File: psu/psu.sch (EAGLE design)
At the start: 7 parts

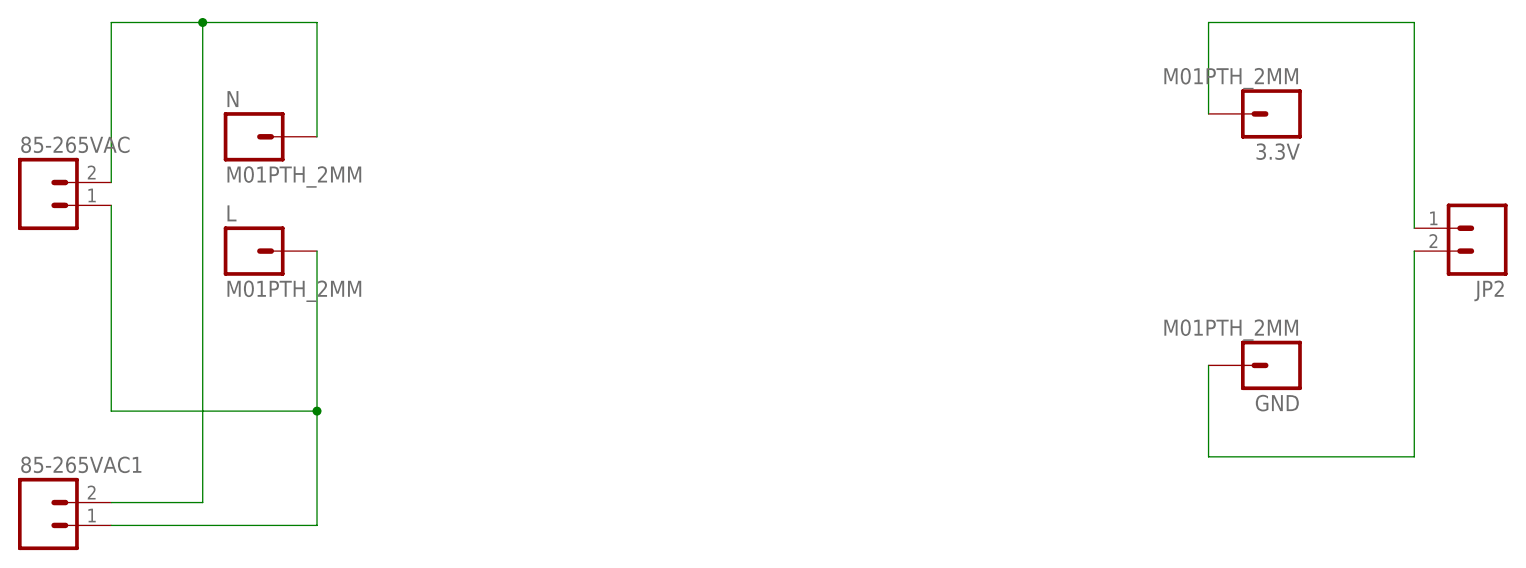
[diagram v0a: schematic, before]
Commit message: psu pcb: smaller holes for psu module
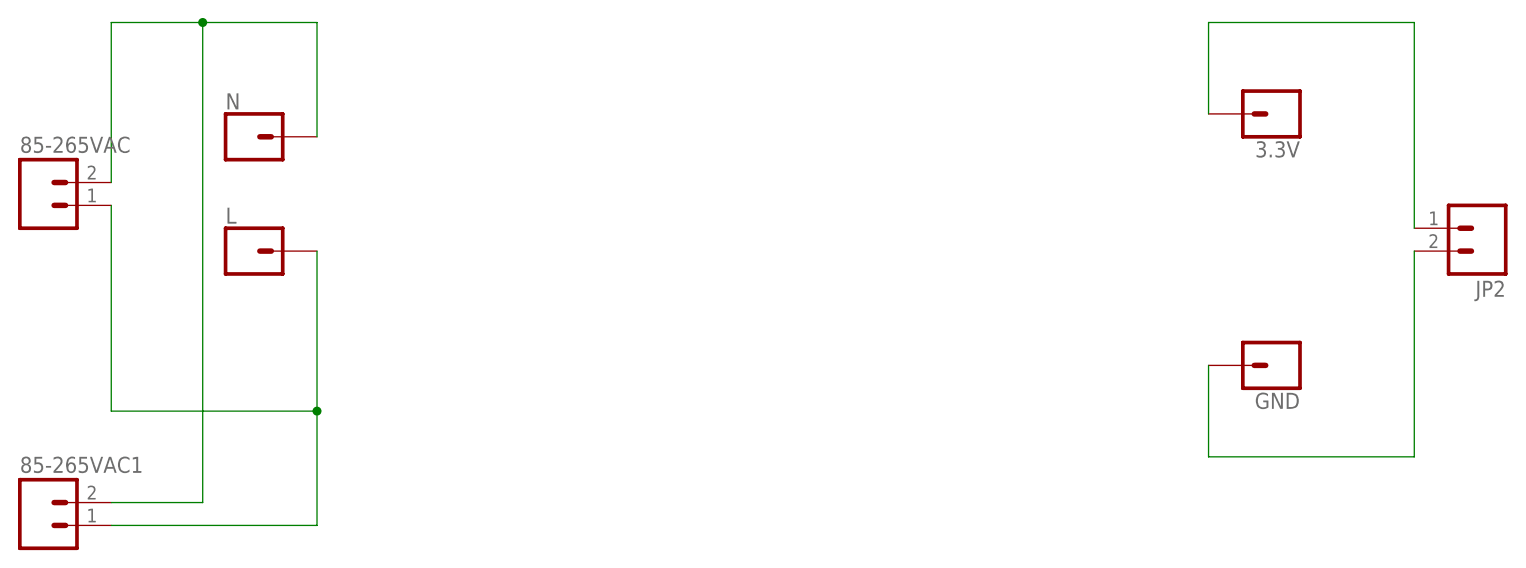
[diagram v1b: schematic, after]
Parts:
- 3.3V, GND, L, N: value M01PTH_2MM -> (none); device SparkFun (old):M01PTH_2MM -> 1X01:CONN_01PTH_1.4MM
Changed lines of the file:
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@@
 <?xml version="1.0" encoding="utf-8"?>
 <!DOCTYPE eagle SYSTEM "eagle.dtd">
-<eagle version="7.2.0">
+<eagle version="8.7.1">
 <drawing>
 <settings>
-<setting alwaysvectorfont="yes"/>
+<setting alwaysvectorfont="no"/>
+<setting keepoldvectorfont="yes"/>
 <setting verticaltext="up"/>
 </settings>
@@
 <layer number="54" name="bGND_GNDA" color="1" fill="9" visible="no" active="no"/>
 <layer number="56" name="wert" color="7" fill="1" visible="no" active="no"/>
+<layer number="57" name="tCAD" color="7" fill="1" visible="no" active="no"/>
+<layer number="59" name="tCarbon" color="7" fill="1" visible="no" active="no"/>
+<layer number="60" name="bCarbon" color="7" fill="1" visible="no" active="no"/>
 <layer number="90" name="Modules" color="5" fill="1" visible="yes" active="yes"/>
 <layer number="91" name="Nets" color="2" fill="1" visible="yes" active="yes"/>
@@
 <layer number="97" name="Info" color="7" fill="1" visible="yes" active="yes"/>
 <layer number="98" name="Guide" color="6" fill="1" visible="yes" active="yes"/>
+<layer number="99" name="SpiceOrder" color="7" fill="1" visible="yes" active="yes"/>
 <layer number="100" name="Muster" color="7" fill="1" visible="no" active="no"/>
 <layer number="101" name="Patch_Top" color="12" fill="4" visible="no" active="yes"/>
@@
 <layer number="106" name="bPlate" color="7" fill="1" visible="no" active="yes"/>
 <layer number="107" name="Crop" color="7" fill="1" visible="no" active="yes"/>
+<layer number="108" name="tplace-old" color="10" fill="1" visible="yes" active="yes"/>
+<layer number="109" name="ref-old" color="11" fill="1" visible="yes" active="yes"/>
+<layer number="110" name="fp0" color="7" fill="1" visible="yes" active="yes"/>
+<layer number="111" name="LPC17xx" color="7" fill="1" visible="yes" active="yes"/>
+<layer number="112" name="tSilk" color="7" fill="1" visible="yes" active="yes"/>
+<layer number="113" name="IDFDebug" color="4" fill="1" visible="yes" active="yes"/>
+<layer number="114" name="Badge_Outline" color="7" fill="1" visible="yes" active="yes"/>
+<layer number="115" name="ReferenceISLANDS" color="7" fill="1" visible="yes" active="yes"/>
 <layer number="116" name="Patch_BOT" color="9" fill="4" visible="no" active="yes"/>
+<layer number="118" name="Rect_Pads" color="7" fill="1" visible="yes" active="yes"/>
 <layer number="121" name="_tsilk" color="7" fill="1" visible="no" active="yes"/>
 <layer number="122" name="_bsilk" color="7" fill="1" visible="no" active="yes"/>
+<layer number="123" name="tTestmark" color="7" fill="1" visible="yes" active="yes"/>
+<layer number="124" name="bTestmark" color="7" fill="1" visible="yes" active="yes"/>
 <layer number="125" name="_tNames" color="7" fill="1" visible="no" active="yes"/>
+<layer number="126" name="_bNames" color="7" fill="1" visible="yes" active="yes"/>
+<layer number="127" name="_tValues" color="7" fill="1" visible="yes" active="yes"/>
+<layer number="128" name="_bValues" color="7" fill="1" visible="yes" active="yes"/>
+<layer number="129" name="Mask" color="7" fill="1" visible="yes" active="yes"/>
+<layer number="131" name="tAdjust" color="7" fill="1" visible="yes" active="yes"/>
+<layer number="132" name="bAdjust" color="7" fill="1" visible="yes" active="yes"/>
 <layer number="144" name="Drill_legend" color="7" fill="1" visible="no" active="yes"/>
+<layer number="150" name="Notes" color="7" fill="1" visible="yes" active="yes"/>
 <layer number="151" name="HeatSink" color="7" fill="1" visible="no" active="yes"/>
+<layer number="152" name="_bDocu" color="7" fill="1" visible="yes" active="yes"/>
+<layer number="153" name="FabDoc1" color="7" fill="1" visible="yes" active="yes"/>
+<layer number="154" name="FabDoc2" color="7" fill="1" visible="yes" active="yes"/>
+<layer number="155" name="FabDoc3" color="7" fill="1" visible="yes" active="yes"/>
+<layer number="199" name="Contour" color="7" fill="1" visible="yes" active="yes"/>
 <layer number="200" name="200bmp" color="1" fill="10" visible="no" active="yes"/>
 <layer number="201" name="201bmp" color="2" fill="10" visible="no" active="yes"/>
@@
 <layer number="223" name="223bmp" color="24" fill="1" visible="no" active="no"/>
 <layer number="224" name="224bmp" color="25" fill="1" visible="no" active="no"/>
+<layer number="225" name="225bmp" color="7" fill="1" visible="yes" active="yes"/>
+<layer number="226" name="226bmp" color="7" fill="1" visible="yes" active="yes"/>
+<layer number="227" name="227bmp" color="7" fill="1" visible="yes" active="yes"/>
+<layer number="228" name="228bmp" color="7" fill="1" visible="yes" active="yes"/>
+<layer number="229" name="229bmp" color="7" fill="1" visible="yes" active="yes"/>
+<layer number="230" name="230bmp" color="7" fill="1" visible="yes" active="yes"/>
+<layer number="231" name="231bmp" color="7" fill="1" visible="yes" active="yes"/>
+<layer number="232" name="Eagle3D_PG2" color="7" fill="1" visible="yes" active="yes"/>
+<layer number="233" name="Eagle3D_PG3" color="7" fill="1" visible="yes" active="yes"/>
+<layer number="248" name="Housing" color="7" fill="1" visible="yes" active="yes"/>
+<layer number="249" name="Edge" color="7" fill="1" visible="yes" active="yes"/>
 <layer number="250" name="Descript" color="3" fill="1" visible="no" active="no"/>
 <layer number="251" name="SMDround" color="12" fill="11" visible="no" active="no"/>
 <layer number="254" name="cooling" color="7" fill="1" visible="no" active="yes"/>
+<layer number="255" name="routoute" color="7" fill="1" visible="yes" active="yes"/>
 </layers>
 <schematic xreflabel="%F%N/%S.%C%R" xrefpart="/%S.%C%R">
@@
 </classes>
 <parts>
-<part name="N" library="SparkFun (old)" deviceset="M01" device="PTH_2MM"/>
-<part name="L" library="SparkFun (old)" deviceset="M01" device="PTH_2MM"/>
-<part name="3.3V" library="SparkFun (old)" deviceset="M01" device="PTH_2MM"/>
-<part name="GND" library="SparkFun (old)" deviceset="M01" device="PTH_2MM"/>
+<part name="N" library="1X01" deviceset="CONN_01" device="PTH_1.4MM" package3d_urn="urn:adsk.eagle:package:38029/1"/>
+<part name="L" library="1X01" deviceset="CONN_01" device="PTH_1.4MM" package3d_urn="urn:adsk.eagle:package:38029/1"/>
+<part name="3.3V" library="1X01" deviceset="CONN_01" device="PTH_1.4MM" package3d_urn="urn:adsk.eagle:package:38029/1"/>
+<part name="GND" library="1X01" deviceset="CONN_01" device="PTH_1.4MM" package3d_urn="urn:adsk.eagle:package:38029/1"/>
 <part name="85-265VAC" library="SparkFun (old)" deviceset="M02" device="PTH3_5MM"/>
 <part name="JP2" library="SparkFun (old)" deviceset="M02" device="PTH3_5MM"/>
@@
 </schematic>
 </drawing>
+<compatibility>
+<note version="8.3" severity="warning">
+Since Version 8.3, EAGLE supports URNs for individual library
+assets (packages, symbols, and devices). The URNs of those assets
+will not be understood (or retained) with this version.
+</note>
+<note version="8.3" severity="warning">
+Since Version 8.3, EAGLE supports the association of 3D packages
+with devices in libraries, schematics, and board files. Those 3D
+packages will not be understood (or retained) with this version.
+</note>
+</compatibility>
 </eagle>
